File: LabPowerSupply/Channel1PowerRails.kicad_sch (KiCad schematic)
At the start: 8 parts

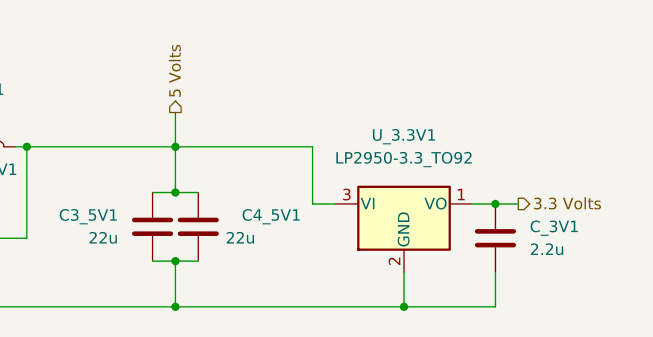
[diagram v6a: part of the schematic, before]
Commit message: Changed grid size, began regrouping
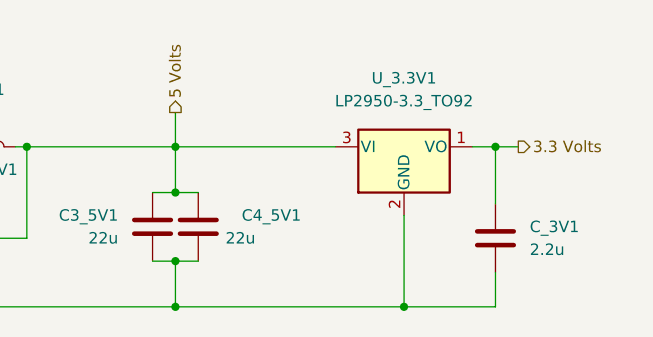
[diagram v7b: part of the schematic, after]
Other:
- moved on the sheet: U_3.3V1
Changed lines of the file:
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@@
   (junction (at 124.46 106.68) (diameter 0) (color 0 0 0 0)
+  )
+  (junction (at 207.01 88.9) (diameter 0) (color 0 0 0 0)
   )
   (junction (at 171.45 93.98) (diameter 0) (color 0 0 0 0)
   )
   (junction (at 196.85 106.68) (diameter 0) (color 0 0 0 0)
-  )
-  (junction (at 207.01 95.25) (diameter 0) (color 0 0 0 0)
   )
   (junction (at 143.51 88.9) (diameter 0) (color 0 0 0 0)
@@
     (stroke (width 0) (type default) (color 0 0 0 0))
   )
+  (wire (pts (xy 171.45 88.9) (xy 189.23 88.9))
+    (stroke (width 0) (type default) (color 0 0 0 0))
+  )
+  (wire (pts (xy 207.01 95.25) (xy 207.01 88.9))
+    (stroke (width 0) (type default) (color 0 0 0 0))
+  )
   (wire (pts (xy 207.01 106.68) (xy 196.85 106.68))
     (stroke (width 0) (type default) (color 0 0 0 0))
   )
-  (wire (pts (xy 186.69 95.25) (xy 189.23 95.25))
-    (stroke (width 0) (type default) (color 0 0 0 0))
-  )
   (wire (pts (xy 102.87 88.9) (xy 114.3 88.9))
-    (stroke (width 0) (type default) (color 0 0 0 0))
-  )
-  (wire (pts (xy 186.69 88.9) (xy 186.69 95.25))
     (stroke (width 0) (type default) (color 0 0 0 0))
   )
@@
     (stroke (width 0) (type default) (color 0 0 0 0))
   )
-  (wire (pts (xy 207.01 95.25) (xy 209.55 95.25))
+  (wire (pts (xy 168.91 93.98) (xy 171.45 93.98))
     (stroke (width 0) (type default) (color 0 0 0 0))
   )
-  (wire (pts (xy 168.91 93.98) (xy 171.45 93.98))
+  (wire (pts (xy 207.01 88.9) (xy 204.47 88.9))
+    (stroke (width 0) (type default) (color 0 0 0 0))
+  )
+  (wire (pts (xy 207.01 88.9) (xy 209.55 88.9))
     (stroke (width 0) (type default) (color 0 0 0 0))
   )
@@
     (stroke (width 0) (type default) (color 0 0 0 0))
   )
-  (wire (pts (xy 171.45 88.9) (xy 186.69 88.9))
-    (stroke (width 0) (type default) (color 0 0 0 0))
-  )
   (wire (pts (xy 171.45 85.09) (xy 171.45 88.9))
     (stroke (width 0) (type default) (color 0 0 0 0))
   )
-  (wire (pts (xy 196.85 106.68) (xy 196.85 102.87))
+  (wire (pts (xy 196.85 106.68) (xy 196.85 96.52))
     (stroke (width 0) (type default) (color 0 0 0 0))
   )
@@
   )
   (wire (pts (xy 102.87 106.68) (xy 124.46 106.68))
-    (stroke (width 0) (type default) (color 0 0 0 0))
-  )
-  (wire (pts (xy 204.47 95.25) (xy 207.01 95.25))
     (stroke (width 0) (type default) (color 0 0 0 0))
   )
@@
     (effects (font (size 1.27 1.27)) (justify right))
   )
-  (hierarchical_label "3.3 Volts" (shape output) (at 209.55 95.25 0)
+  (hierarchical_label "3.3 Volts" (shape output) (at 209.55 88.9 0)
     (effects (font (size 1.27 1.27)) (justify left))
   )
@@
     (pin "2")
   )
-  (symbol (lib_id "Regulator_Linear:LP2950-3.3_TO92") (at 196.85 95.25 0) (unit 1)
+  (symbol (lib_id "Regulator_Linear:LP2950-3.3_TO92") (at 196.85 88.9 0) (unit 1)
     (in_bom yes) (on_board yes) (fields_autoplaced)
-    (property "Reference" "U_3.3V1" (id 0) (at 196.85 87.63 0))
-    (property "Value" "LP2950-3.3_TO92" (id 1) (at 196.85 90.17 0))
-    (property "Footprint" "Package_TO_SOT_SMD:TO-252-3_TabPin4" (id 2) (at 196.85 89.535 0)
+    (property "Reference" "U_3.3V1" (id 0) (at 196.85 81.28 0))
+    (property "Value" "LP2950-3.3_TO92" (id 1) (at 196.85 83.82 0))
+    (property "Footprint" "Package_TO_SOT_SMD:TO-252-3_TabPin4" (id 2) (at 196.85 83.185 0)
       (effects (font (size 1.27 1.27) italic) hide)
     )
-    (property "Datasheet" "http://www.ti.com/lit/ds/symlink/lp2950.pdf" (id 3) (at 196.85 96.52 0)
+    (property "Datasheet" "http://www.ti.com/lit/ds/symlink/lp2950.pdf" (id 3) (at 196.85 90.17 0)
       (effects (font (size 1.27 1.27)) hide)
     )

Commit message: routing is weird
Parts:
- renumbered C4_5V1 to C1_3V1, C_3V1 to C2_3V1, U_3.3V1 to U_3V1
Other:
- moved on the sheet: C1_3V1, C3_5V1
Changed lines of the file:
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@@
     (comment 4 "This supplys the 5 volts and 3.3 volts rail for the primary digital")
   )
-  (junction (at 171.45 106.68) (diameter 0) (color 0 0 0 0)
-  )
-  (junction (at 171.45 101.6) (diameter 0) (color 0 0 0 0)
-  )
-  (junction (at 171.45 88.9) (diameter 0) (color 0 0 0 0)
-  )
   (junction (at 102.87 106.68) (diameter 0) (color 0 0 0 0)
   )
@@
   (junction (at 207.01 88.9) (diameter 0) (color 0 0 0 0)
   )
-  (junction (at 171.45 93.98) (diameter 0) (color 0 0 0 0)
-  )
   (junction (at 196.85 106.68) (diameter 0) (color 0 0 0 0)
   )
+  (junction (at 167.64 88.9) (diameter 0) (color 0 0 0 0)
+  )
+  (junction (at 181.61 88.9) (diameter 0) (color 0 0 0 0)
+  )
+  (junction (at 181.61 106.68) (diameter 0) (color 0 0 0 0)
+  )
+  (junction (at 167.64 106.68) (diameter 0) (color 0 0 0 0)
+  )
   (junction (at 143.51 88.9) (diameter 0) (color 0 0 0 0)
   )
@@
   (junction (at 154.94 88.9) (diameter 0) (color 0 0 0 0)
   )
-  (wire (pts (xy 168.91 101.6) (xy 171.45 101.6))
-    (stroke (width 0) (type default) (color 0 0 0 0))
-  )
-  (wire (pts (xy 171.45 88.9) (xy 189.23 88.9))
+  (wire (pts (xy 167.64 88.9) (xy 181.61 88.9))
     (stroke (width 0) (type default) (color 0 0 0 0))
   )
@@
     (stroke (width 0) (type default) (color 0 0 0 0))
   )
+  (wire (pts (xy 181.61 88.9) (xy 181.61 93.98))
+    (stroke (width 0) (type default) (color 0 0 0 0))
+  )
   (wire (pts (xy 97.79 88.9) (xy 102.87 88.9))
     (stroke (width 0) (type default) (color 0 0 0 0))
@@
     (stroke (width 0) (type default) (color 0 0 0 0))
   )
-  (wire (pts (xy 168.91 93.98) (xy 171.45 93.98))
-    (stroke (width 0) (type default) (color 0 0 0 0))
-  )
   (wire (pts (xy 207.01 88.9) (xy 204.47 88.9))
     (stroke (width 0) (type default) (color 0 0 0 0))
@@
     (stroke (width 0) (type default) (color 0 0 0 0))
   )
+  (wire (pts (xy 181.61 101.6) (xy 181.61 106.68))
+    (stroke (width 0) (type default) (color 0 0 0 0))
+  )
+  (wire (pts (xy 167.64 101.6) (xy 167.64 106.68))
+    (stroke (width 0) (type default) (color 0 0 0 0))
+  )
   (wire (pts (xy 114.3 88.9) (xy 114.3 93.98))
     (stroke (width 0) (type default) (color 0 0 0 0))
@@
     (stroke (width 0) (type default) (color 0 0 0 0))
   )
+  (wire (pts (xy 167.64 106.68) (xy 181.61 106.68))
+    (stroke (width 0) (type default) (color 0 0 0 0))
+  )
   (wire (pts (xy 207.01 102.87) (xy 207.01 106.68))
     (stroke (width 0) (type default) (color 0 0 0 0))
@@
     (stroke (width 0) (type default) (color 0 0 0 0))
   )
-  (wire (pts (xy 171.45 101.6) (xy 171.45 106.68))
-    (stroke (width 0) (type default) (color 0 0 0 0))
-  )
-  (wire (pts (xy 154.94 88.9) (xy 171.45 88.9))
-    (stroke (width 0) (type default) (color 0 0 0 0))
-  )
-  (wire (pts (xy 171.45 106.68) (xy 196.85 106.68))
+  (wire (pts (xy 154.94 88.9) (xy 167.64 88.9))
+    (stroke (width 0) (type default) (color 0 0 0 0))
+  )
+  (wire (pts (xy 181.61 106.68) (xy 196.85 106.68))
+    (stroke (width 0) (type default) (color 0 0 0 0))
+  )
+  (wire (pts (xy 167.64 88.9) (xy 167.64 93.98))
     (stroke (width 0) (type default) (color 0 0 0 0))
   )
@@
     (stroke (width 0) (type default) (color 0 0 0 0))
   )
-  (wire (pts (xy 171.45 85.09) (xy 171.45 88.9))
+  (wire (pts (xy 167.64 85.09) (xy 167.64 88.9))
+    (stroke (width 0) (type default) (color 0 0 0 0))
+  )
+  (wire (pts (xy 181.61 88.9) (xy 189.23 88.9))
     (stroke (width 0) (type default) (color 0 0 0 0))
   )
@@
     (stroke (width 0) (type default) (color 0 0 0 0))
   )
-  (wire (pts (xy 171.45 93.98) (xy 173.99 93.98))
-    (stroke (width 0) (type default) (color 0 0 0 0))
-  )
-  (wire (pts (xy 124.46 106.68) (xy 171.45 106.68))
-    (stroke (width 0) (type default) (color 0 0 0 0))
-  )
-  (wire (pts (xy 171.45 101.6) (xy 173.99 101.6))
+  (wire (pts (xy 124.46 106.68) (xy 167.64 106.68))
     (stroke (width 0) (type default) (color 0 0 0 0))
   )
   (wire (pts (xy 153.67 88.9) (xy 154.94 88.9))
-    (stroke (width 0) (type default) (color 0 0 0 0))
-  )
-  (wire (pts (xy 171.45 88.9) (xy 171.45 93.98))
     (stroke (width 0) (type default) (color 0 0 0 0))
   )
@@
     (effects (font (size 1.27 1.27)) (justify right))
   )
-  (hierarchical_label "5 Volts" (shape output) (at 171.45 85.09 90)
+  (hierarchical_label "5 Volts" (shape output) (at 167.64 85.09 90)
     (effects (font (size 1.27 1.27)) (justify left))
   )
-  (symbol (lib_id "Device:C") (at 173.99 97.79 0) (mirror x) (unit 1)
+  (symbol (lib_id "Device:C") (at 181.61 97.79 0) (mirror x) (unit 1)
     (in_bom yes) (on_board yes)
-    (property "Reference" "C4_5V1" (id 0) (at 185.42 96.52 0)
-      (effects (font (size 1.27 1.27)) (justify right))
-    )
-    (property "Value" "22u" (id 1) (at 180.34 99.06 0)
-      (effects (font (size 1.27 1.27)) (justify right))
-    )
-    (property "Footprint" "Capacitor_SMD:C_1210_3225Metric" (id 2) (at 174.9552 93.98 0)
-      (effects (font (size 1.27 1.27)) hide)
-    )
-    (property "Datasheet" "~" (id 3) (at 173.99 97.79 0)
+    (property "Reference" "C1_3V1" (id 0) (at 193.04 96.52 0)
+      (effects (font (size 1.27 1.27)) (justify right))
+    )
+    (property "Value" "22u" (id 1) (at 187.96 99.06 0)
+      (effects (font (size 1.27 1.27)) (justify right))
+    )
+    (property "Footprint" "Capacitor_SMD:C_1210_3225Metric" (id 2) (at 182.5752 93.98 0)
+      (effects (font (size 1.27 1.27)) hide)
+    )
+    (property "Datasheet" "~" (id 3) (at 181.61 97.79 0)
       (effects (font (size 1.27 1.27)) hide)
     )
@@
   (symbol (lib_id "Device:C") (at 207.01 99.06 0) (unit 1)
     (in_bom yes) (on_board yes) (fields_autoplaced)
-    (property "Reference" "C_3V1" (id 0) (at 210.82 97.7899 0)
+    (property "Reference" "C2_3V1" (id 0) (at 210.82 97.7899 0)
       (effects (font (size 1.27 1.27)) (justify left))
     )
@@
   (symbol (lib_id "Regulator_Linear:LP2950-3.3_TO92") (at 196.85 88.9 0) (unit 1)
     (in_bom yes) (on_board yes) (fields_autoplaced)
-    (property "Reference" "U_3.3V1" (id 0) (at 196.85 81.28 0))
+    (property "Reference" "U_3V1" (id 0) (at 196.85 81.28 0))
     (property "Value" "LP2950-3.3_TO92" (id 1) (at 196.85 83.82 0))
     (property "Footprint" "Package_TO_SOT_SMD:TO-252-3_TabPin4" (id 2) (at 196.85 83.185 0)
@@
     (pin "2")
   )
-  (symbol (lib_id "Device:C") (at 168.91 97.79 0) (mirror x) (unit 1)
-    (in_bom yes) (on_board yes) (fields_autoplaced)
-    (property "Reference" "C3_5V1" (id 0) (at 165.1 96.5199 0)
-      (effects (font (size 1.27 1.27)) (justify right))
-    )
-    (property "Value" "22u" (id 1) (at 165.1 99.0599 0)
-      (effects (font (size 1.27 1.27)) (justify right))
-    )
-    (property "Footprint" "Capacitor_SMD:C_1210_3225Metric" (id 2) (at 169.8752 93.98 0)
-      (effects (font (size 1.27 1.27)) hide)
-    )
-    (property "Datasheet" "~" (id 3) (at 168.91 97.79 0)
-      (effects (font (size 1.27 1.27)) hide)
-    )
+  (symbol (lib_id "Device:C") (at 167.64 97.79 0) (mirror x) (unit 1)
+    (in_bom yes) (on_board yes) (fields_autoplaced)
+    (property "Reference" "C3_5V1" (id 0) (at 163.83 96.5199 0)
+      (effects (font (size 1.27 1.27)) (justify right))
+    )
+    (property "Value" "22u" (id 1) (at 163.83 99.0599 0)
+      (effects (font (size 1.27 1.27)) (justify right))
+    )
+    (property "Footprint" "Capacitor_SMD:C_1210_3225Metric" (id 2) (at 168.6052 93.98 0)
+      (effects (font (size 1.27 1.27)) hide)
+    )
+    (property "Datasheet" "~" (id 3) (at 167.64 97.79 0)
+      (effects (font (size 1.27 1.27)) hide)
+    )
